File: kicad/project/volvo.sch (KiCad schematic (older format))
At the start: 1 part, among them U1 LM324

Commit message: Trace in progress.
..
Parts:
- added C1: 33µ, symbol CP
- added C2: 33n, symbol C
- added C3, C5: 1µ, symbol CP
- added C4: 2.1n, symbol C
- added C6: 58n, symbol C
- added D1, D3: DIODE, symbol DIODE
- added D4: tiny, symbol DIODE
- added FU: FUSE, symbol FUSE
- added Q1, Q3: C1740, SOT-23, symbol BC850
- added Q2: POWER, SOT-23, symbol BC850
- added Q4: BC850, SOT-23, symbol BC850
- added R1, R11, R12, R2: 33k, symbol R
- added R10: 1k, symbol R
- added R13: 105, symbol R
- added R3, R9: 10k, symbol R
- added R4: 110k, symbol R
- added R5: 470, symbol R
- added R6: 220, symbol R
- added R7: 271, symbol R
- added R8: 200, symbol R
- added RV?: POT, symbol POT
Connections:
- net GND: now reaches U1.11 (V-)
- net GND: now also U1.10 (+), U1.11 (V-), U1.11 (V-), U1.11 (V-), C1.2, C2.2, C5.2, D3.1 (A), D4.1 (A), Q2.2 (E), R2.2
- net at U1.2 (-): now also Q1.1 (B), R13.1
- net at U1.3 (+): now also R11.2, R12.1
- net VCC: now reaches U1.4 (V+)
- net VCC: now also U1.4 (V+), U1.4 (V+), U1.4 (V+), C1.1, D1.2 (K), Q1.3 (C), R1.1, R11.1
- net at U1.12 (+): now also R1.2, R2.1, R3.2
- net at U1.13 (-): now also U1.6 (-), C2.1, R4.2
- net at U1.14: now also C6.2, R3.1, R4.1
- new net: U1.8, U1.9 (-)
- new net: Q1.2 (E), R7.1
- new net: Q2.3 (C), Q3.3 (C), R7.2, R8.1
- new net: C4.2, Q3.2 (E), R10.2, R12.2, R8.2
- new net: D3.2 (K), FU.1, Q2.1 (B), R9.1
- new net: C4.1, C6.1, Q3.1 (B), R10.1, R9.2
- new net OUT_TERMINAL: FU.2
- new net POT_TERMINAL: C5.1, D4.2 (K), U1.5 (+)
- new net VCC_TERMINAL: D1.1 (A)
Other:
- note added: "UMI 12 x22\n3A 250V"
- moved on the sheet: U1A, U1D

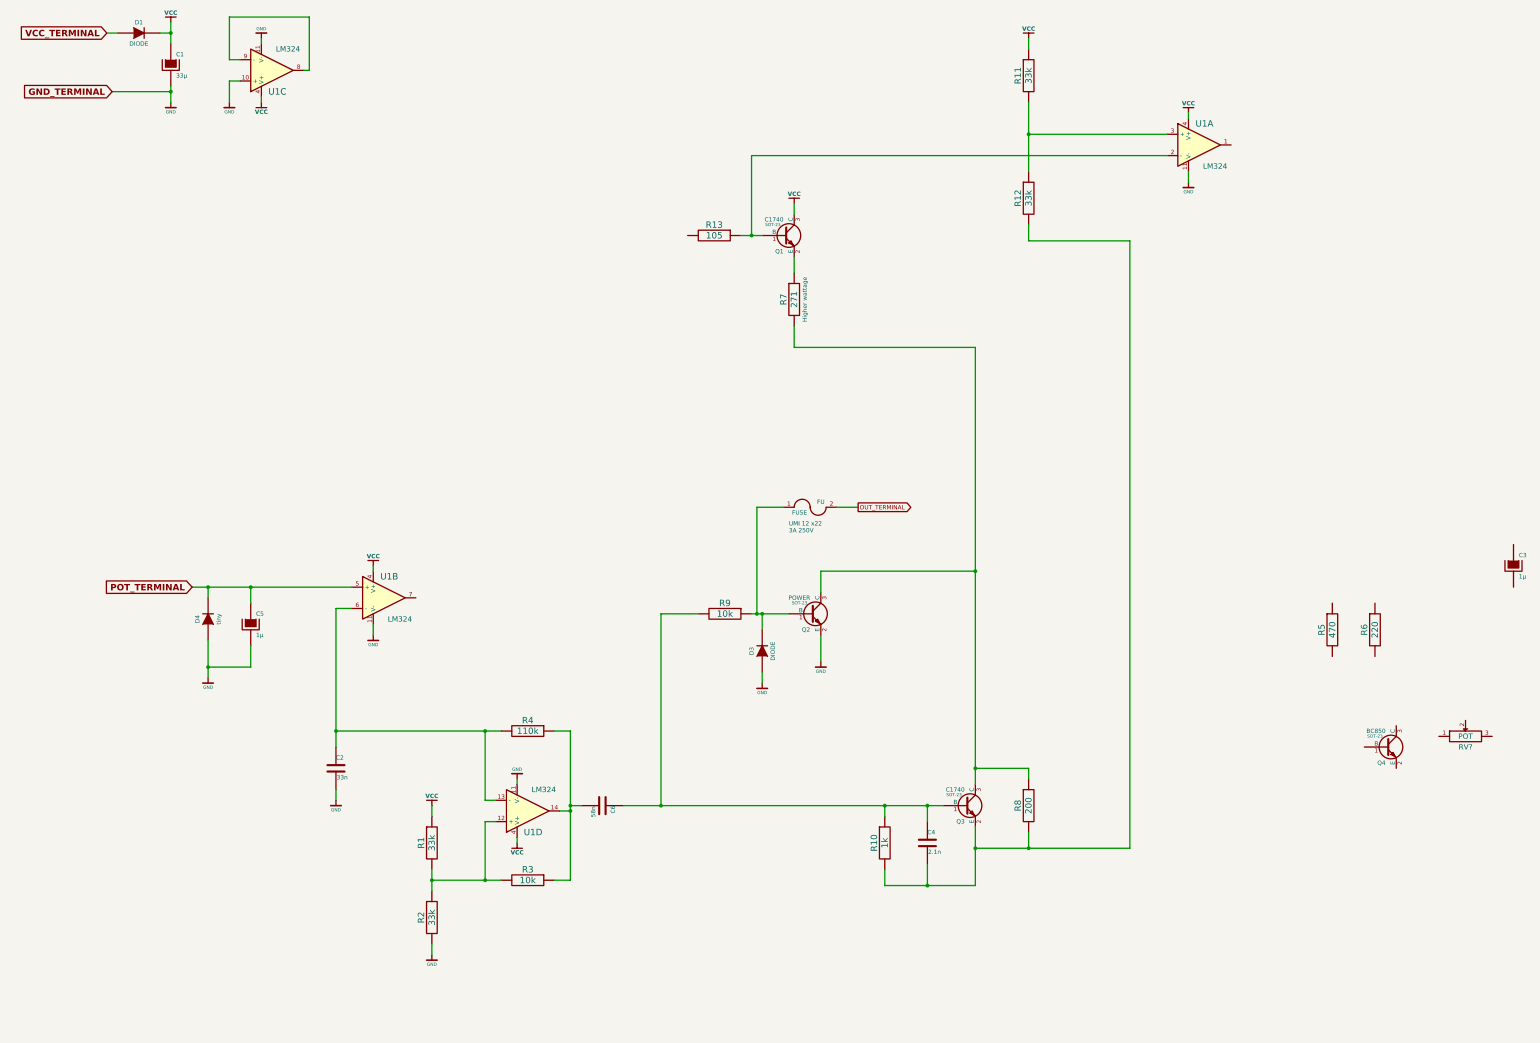
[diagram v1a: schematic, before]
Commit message: All connections traced.
All connections traced, still mostly unverified.
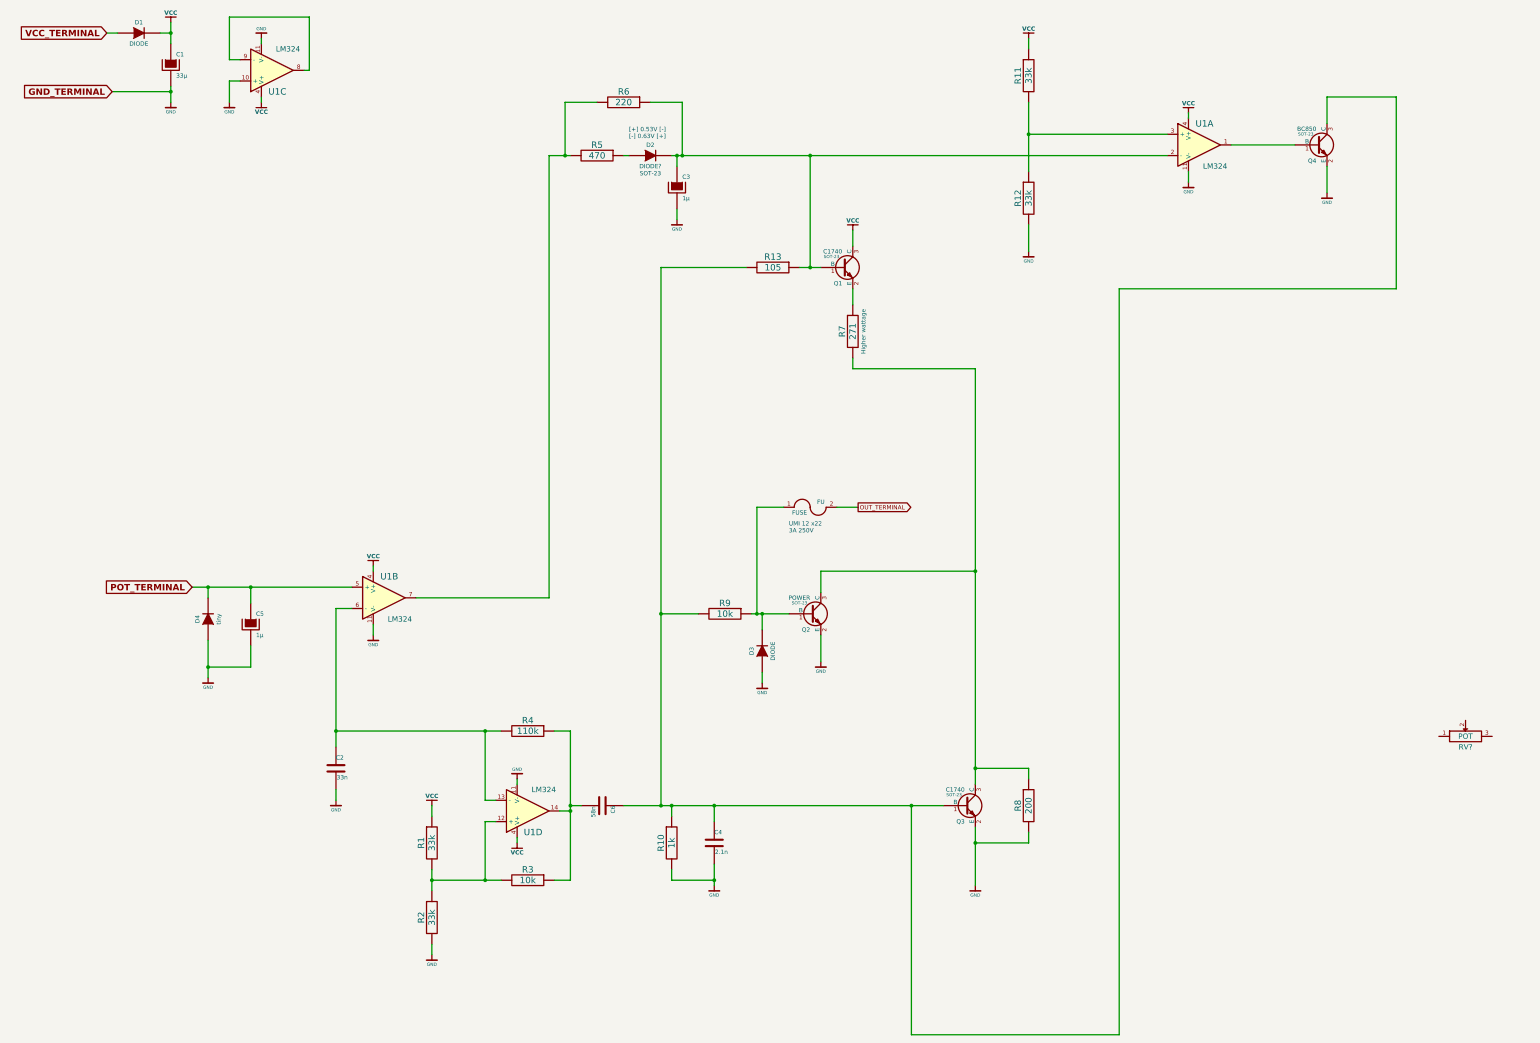
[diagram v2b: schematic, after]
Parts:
- added D2: DIODE?, symbol DIODE
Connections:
- net GND: now also C3.2, C4.2, Q3.2 (E), Q4.2 (E), R10.2, R12.2, R8.2
- net at U1.1: now also Q4.1 (B)
- net at Q1.1 (B), R13.1, U1.2 (-): now also C3.1, R6.1, D2.2 (K)
- net at U1.7: now also R5.2, R6.2
- net at R5.1: now also D2.1 (A)
- net at C4.1, C6.1, Q3.1 (B)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: now also Q4.3 (C), R13.2
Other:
- note added: "SOT-23"
- note added: "[+] 0.53V [-]\n[-] 0.63V [+]"
- moved on the sheet: C3, C4, Q1, Q4, R10, R13, R5, R6, R7

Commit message: First release.
Schematic cleanup. First PDF plot.
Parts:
- removed RV?: POT, symbol POT
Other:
- moved on the sheet: C1, C2, C3, C4, C5, C6, D1, D2, D3, D4, FU, Q1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

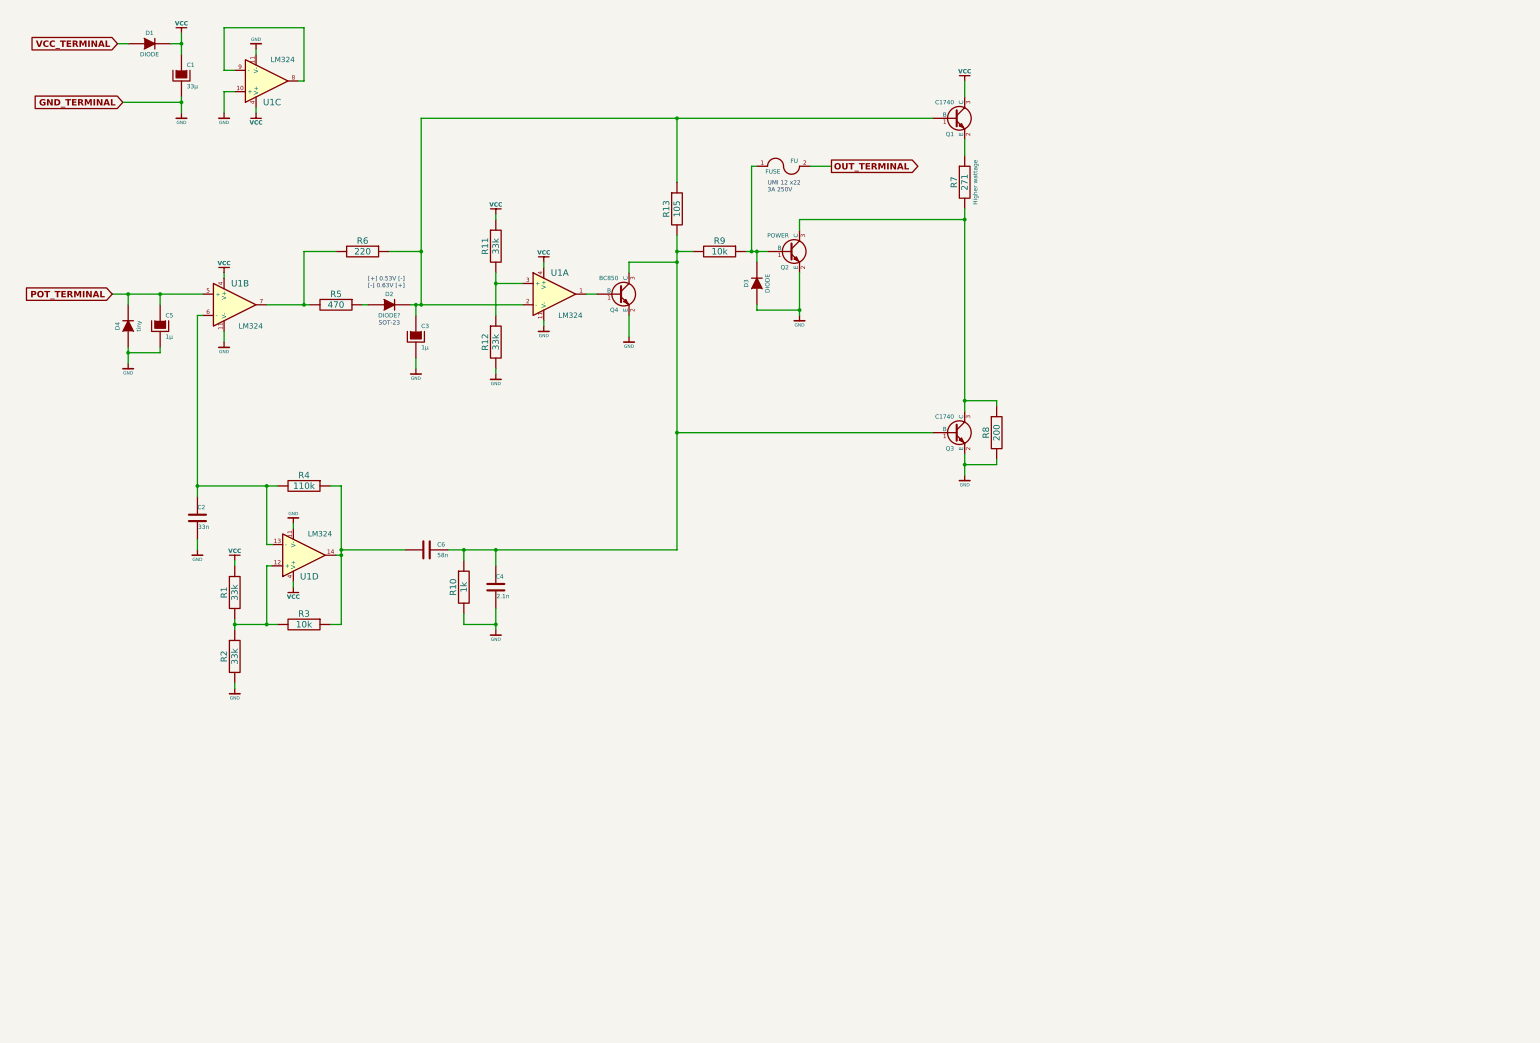
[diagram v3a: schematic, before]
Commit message: Update schematic and trace image.
- Fixed power transistor pinout.
- Major schematic redraw.
- Checked connections drawn in red.
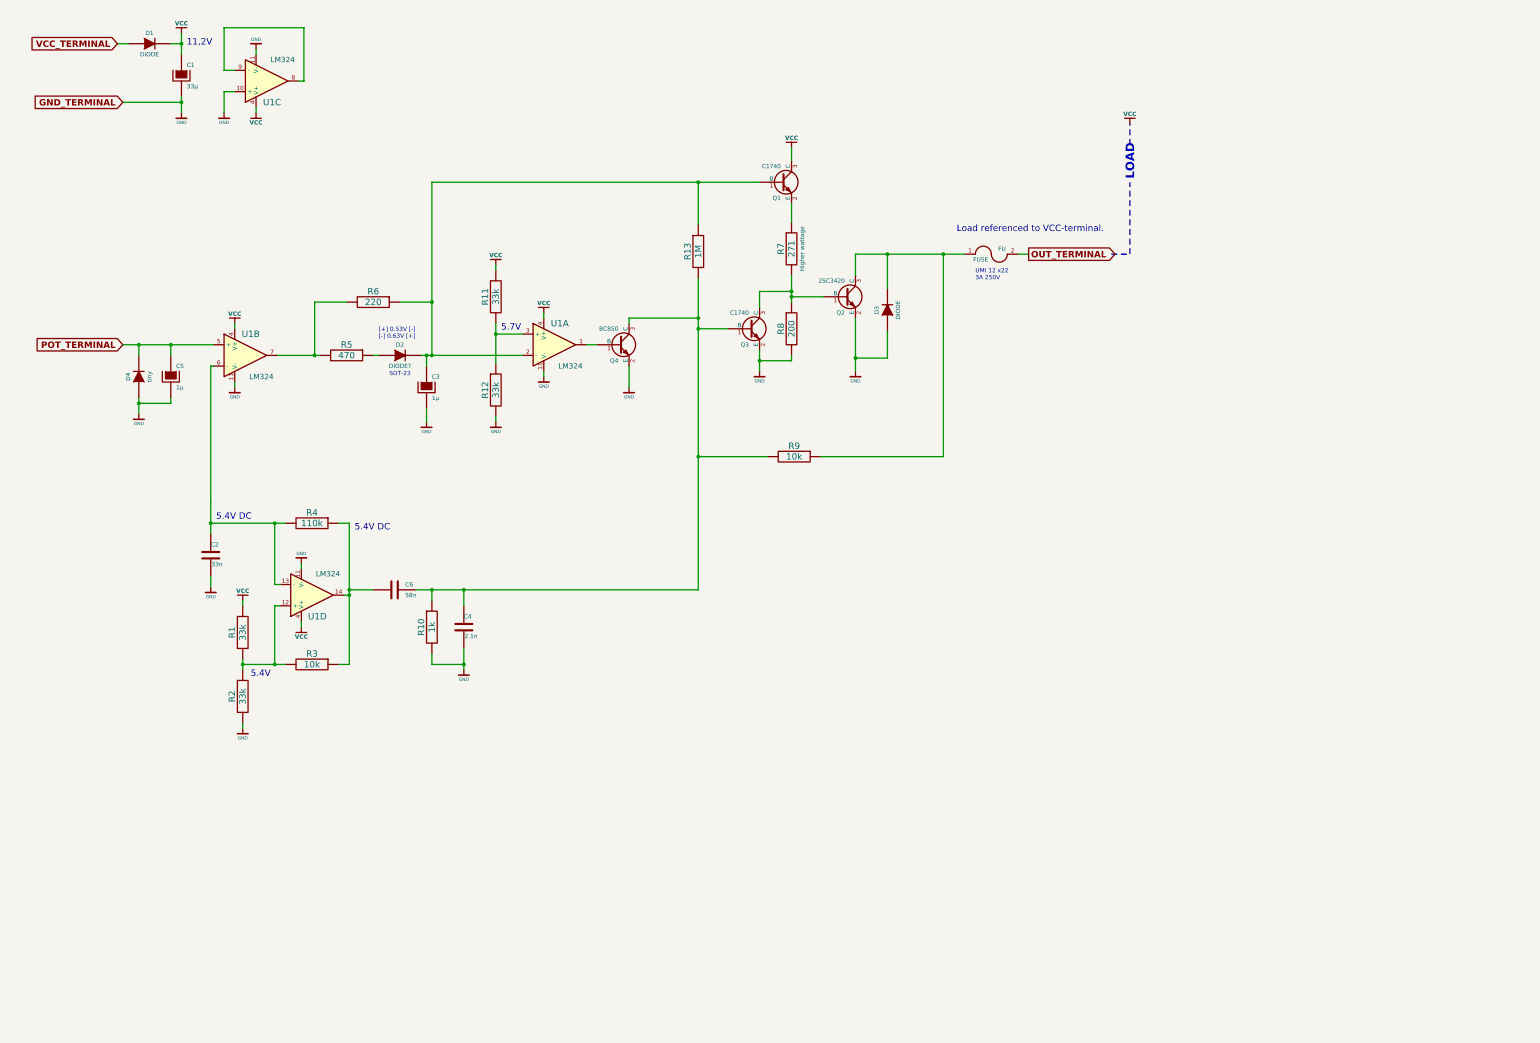
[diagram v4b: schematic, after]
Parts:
- Q2: value POWER -> 2SC3420
- R13: value 105 -> 1M
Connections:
- net at Q3.3 (C), R7.2, R8.1: now also Q2.1 (B); no longer Q2.3 (C)
- net at D3.2 (K), FU.1, R9.1: now also Q2.3 (C); no longer Q2.1 (B)
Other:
- note added: "11,2V"
- note added: "5.4V"
- note added: "5.4V DC"
- note added: "5.7V"
- note added: "LOAD"
- note added: "Load referenced to VCC-terminal."
- moved on the sheet: C2, C3, C4, C5, C6, D2, D3, D4, FU, Q1, Q2, Q3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
